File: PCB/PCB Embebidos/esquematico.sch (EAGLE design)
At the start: 14 parts, among them T1 BT138-V

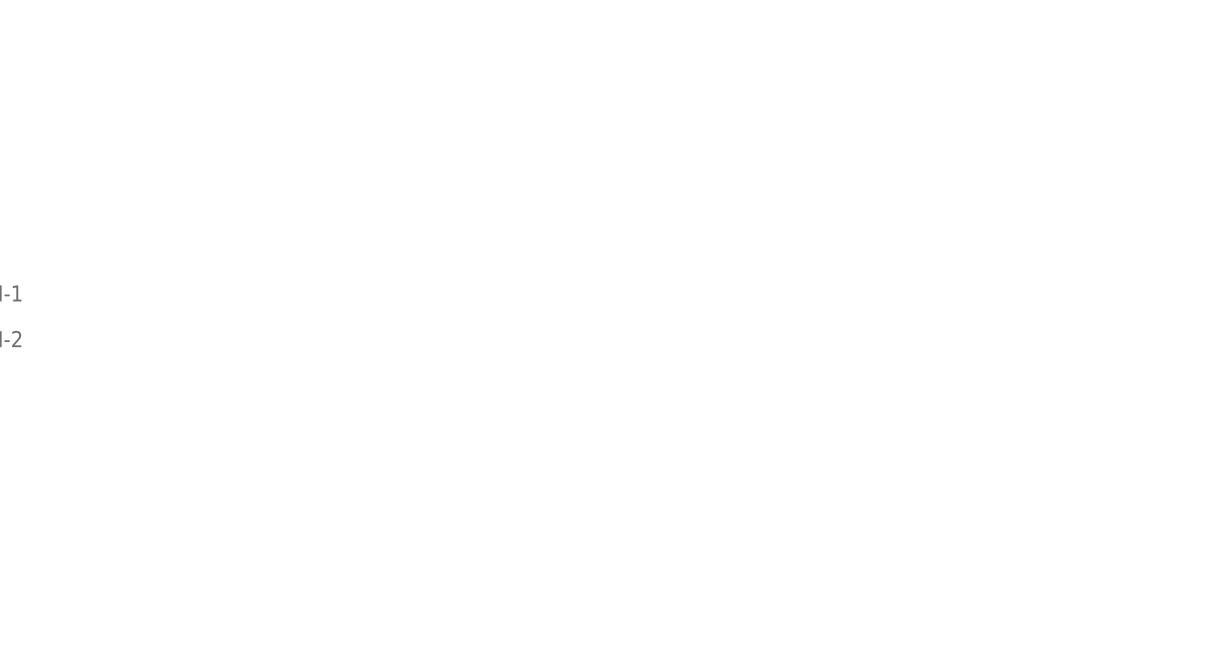
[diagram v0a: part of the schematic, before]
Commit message: Agregue el circuito de la termocupla al esquematico de Eagle. Falta definir si vamos a meter el PT100 como referencia
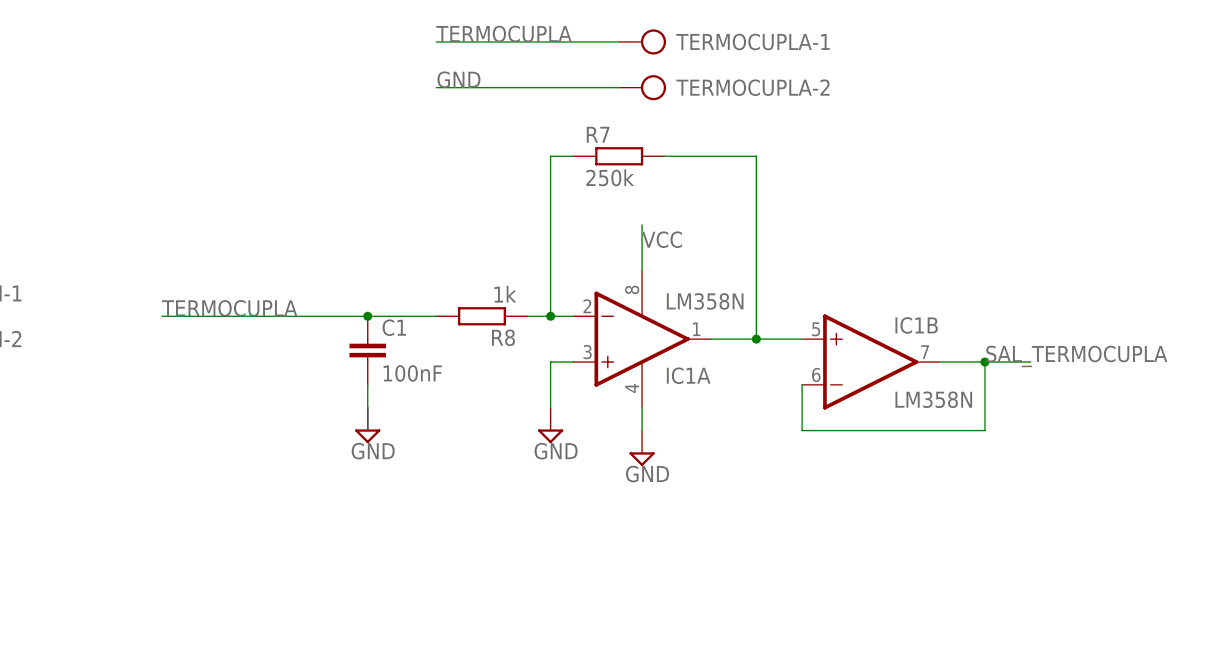
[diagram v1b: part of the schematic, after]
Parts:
- added C1: 100nF, capacitor-wima:C2,5-3
- added IC1: LM358N, linear:LM358N
- added R7: 250k, resistor:R-EU_0207/10
- added R8: 1k, resistor:R-EU_0207/10
- added TERMOCUPLA: (no value), con-ptr500:AK300/2
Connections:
- new net N$5: IC1A.-IN, R7.1, R8.1
- new net N$7: IC1A.OUT, IC1B.+IN, R7.2
- new net SAL_TERMOCUPLA: IC1B.-IN, IC1B.OUT
- new net TERMOCUPLA: C1.1, R8.2, TERMOCUPLA-1.KL
- net GND: now also C1.2, IC1A.+IN, IC1P.V-, TERMOCUPLA-2.KL
- net VCC: now also IC1P.V+
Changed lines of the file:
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@@
 <part name="ALIMENTACION" library="con-ptr500" deviceset="AK300/2" device=""/>
 <part name="PWM-FASE" library="con-ptr500" deviceset="AK300/2" device=""/>
+<part name="TERMOCUPLA" library="con-ptr500" deviceset="AK300/2" device=""/>
+<part name="IC1" library="linear" deviceset="LM358" device="N"/>
+<part name="R7" library="resistor" deviceset="R-EU_" device="0207/10" value="250k"/>
+<part name="C1" library="capacitor-wima" deviceset="C" device="2,5-3" value="100nF"/>
+<part name="R8" library="resistor" deviceset="R-EU_" device="0207/10" value="1k"/>
+<part name="SUPPLY2" library="supply2" deviceset="GND" device=""/>
+<part name="SUPPLY3" library="supply2" deviceset="GND" device=""/>
+<part name="SUPPLY4" library="supply2" deviceset="GND" device=""/>
 </parts>
 <sheets>
@@
 <instance part="PWM-FASE" gate="-1" x="109.22" y="111.76" rot="MR0"/>
 <instance part="PWM-FASE" gate="-2" x="109.22" y="106.68" rot="MR0"/>
+<instance part="TERMOCUPLA" gate="-1" x="200.66" y="124.46" rot="MR0"/>
+<instance part="TERMOCUPLA" gate="-2" x="200.66" y="119.38" rot="MR0"/>
+<instance part="IC1" gate="A" x="198.12" y="91.44" rot="MR180"/>
+<instance part="IC1" gate="B" x="223.52" y="88.9"/>
+<instance part="R7" gate="G$1" x="195.58" y="111.76"/>
+<instance part="C1" gate="G$1" x="167.64" y="91.44"/>
+<instance part="R8" gate="G$1" x="180.34" y="93.98" rot="R180"/>
+<instance part="SUPPLY2" gate="GND" x="167.64" y="81.28"/>
+<instance part="SUPPLY3" gate="GND" x="187.96" y="81.28"/>
+<instance part="IC1" gate="P" x="198.12" y="91.44"/>
+<instance part="SUPPLY4" gate="GND" x="198.12" y="78.74"/>
 </instances>
 <busses>
@@
 <wire x1="48.26" y1="48.26" x2="76.2" y2="48.26" width="0.1524" layer="91"/>
 <label x="48.26" y="48.26" size="1.778" layer="95"/>
+</segment>
+<segment>
+<pinref part="C1" gate="G$1" pin="2"/>
+<wire x1="167.64" y1="86.36" x2="167.64" y2="83.82" width="0.1524" layer="91"/>
+<wire x1="167.64" y1="81.28" x2="167.64" y2="83.82" width="0.1524" layer="91"/>
+<pinref part="SUPPLY2" gate="GND" pin="GND"/>
+</segment>
+<segment>
+<pinref part="TERMOCUPLA" gate="-2" pin="KL"/>
+<wire x1="195.58" y1="119.38" x2="175.26" y2="119.38" width="0.1524" layer="91"/>
+<label x="175.26" y="119.38" size="1.778" layer="95"/>
+</segment>
+<segment>
+<pinref part="IC1" gate="A" pin="+IN"/>
+<pinref part="SUPPLY3" gate="GND" pin="GND"/>
+<wire x1="190.5" y1="88.9" x2="187.96" y2="88.9" width="0.1524" layer="91"/>
+<wire x1="187.96" y1="88.9" x2="187.96" y2="83.82" width="0.1524" layer="91"/>
+</segment>
+<segment>
+<pinref part="IC1" gate="P" pin="V-"/>
+<pinref part="SUPPLY4" gate="GND" pin="GND"/>
+<wire x1="198.12" y1="81.28" x2="198.12" y2="83.82" width="0.1524" layer="91"/>
 </segment>
 </net>
@@
 <label x="71.12" y="124.46" size="1.778" layer="95"/>
 </segment>
+<segment>
+<pinref part="IC1" gate="P" pin="V+"/>
+<wire x1="198.12" y1="99.06" x2="198.12" y2="104.14" width="0.1524" layer="91"/>
+<label x="198.12" y="101.6" size="1.778" layer="95"/>
+</segment>
 </net>
 <net name="FASE" class="0">
@@
 </segment>
 </net>
+<net name="SAL_TERMOCUPLA" class="0">
+<segment>
+<pinref part="IC1" gate="B" pin="OUT"/>
+<wire x1="231.14" y1="88.9" x2="236.22" y2="88.9" width="0.1524" layer="91"/>
+<label x="236.22" y="88.9" size="1.778" layer="95"/>
+<pinref part="IC1" gate="B" pin="-IN"/>
+<wire x1="236.22" y1="88.9" x2="241.3" y2="88.9" width="0.1524" layer="91"/>
+<wire x1="215.9" y1="86.36" x2="215.9" y2="81.28" width="0.1524" layer="91"/>
+<wire x1="215.9" y1="81.28" x2="236.22" y2="81.28" width="0.1524" layer="91"/>
+<wire x1="236.22" y1="81.28" x2="236.22" y2="88.9" width="0.1524" layer="91"/>
+<junction x="236.22" y="88.9"/>
+</segment>
+</net>
+<net name="N$5" class="0">
+<segment>
+<pinref part="R8" gate="G$1" pin="1"/>
+<pinref part="IC1" gate="A" pin="-IN"/>
+<wire x1="185.42" y1="93.98" x2="187.96" y2="93.98" width="0.1524" layer="91"/>
+<pinref part="R7" gate="G$1" pin="1"/>
+<wire x1="187.96" y1="93.98" x2="190.5" y2="93.98" width="0.1524" layer="91"/>
+<wire x1="190.5" y1="111.76" x2="187.96" y2="111.76" width="0.1524" layer="91"/>
+<wire x1="187.96" y1="111.76" x2="187.96" y2="93.98" width="0.1524" layer="91"/>
+<junction x="187.96" y="93.98"/>
+</segment>
+</net>
+<net name="N$7" class="0">
+<segment>
+<pinref part="R7" gate="G$1" pin="2"/>
+<wire x1="200.66" y1="111.76" x2="210.82" y2="111.76" width="0.1524" layer="91"/>
+<wire x1="210.82" y1="111.76" x2="210.82" y2="91.44" width="0.1524" layer="91"/>
+<pinref part="IC1" gate="A" pin="OUT"/>
+<wire x1="210.82" y1="91.44" x2="205.74" y2="91.44" width="0.1524" layer="91"/>
+<pinref part="IC1" gate="B" pin="+IN"/>
+<wire x1="215.9" y1="91.44" x2="210.82" y2="91.44" width="0.1524" layer="91"/>
+<junction x="210.82" y="91.44"/>
+</segment>
+</net>
+<net name="TERMOCUPLA" class="0">
+<segment>
+<pinref part="TERMOCUPLA" gate="-1" pin="KL"/>
+<wire x1="195.58" y1="124.46" x2="175.26" y2="124.46" width="0.1524" layer="91"/>
+<label x="175.26" y="124.46" size="1.778" layer="95"/>
+</segment>
+<segment>
+<pinref part="R8" gate="G$1" pin="2"/>
+<pinref part="C1" gate="G$1" pin="1"/>
+<wire x1="175.26" y1="93.98" x2="167.64" y2="93.98" width="0.1524" layer="91"/>
+<wire x1="167.64" y1="93.98" x2="144.78" y2="93.98" width="0.1524" layer="91"/>
+<junction x="167.64" y="93.98"/>
+<label x="144.78" y="93.98" size="1.778" layer="95"/>
+</segment>
+</net>

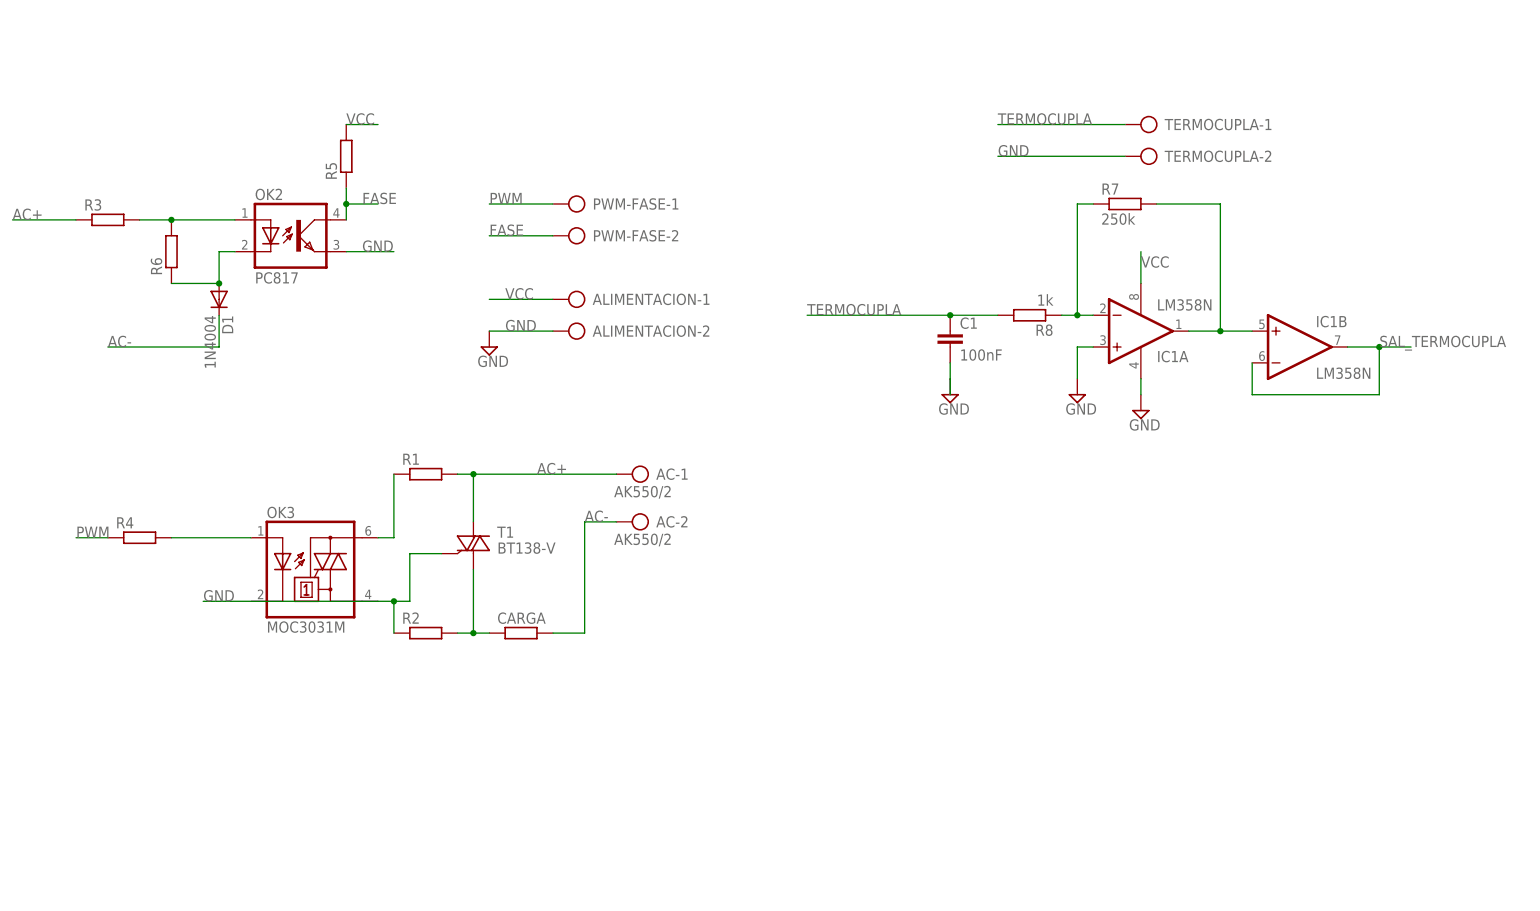
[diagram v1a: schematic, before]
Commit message: Agregue al PCB un regulador de 3.3v porque la EDU-CIAA labura con esa tension, y sino iba a tener problemas con el ADC. Tendria que probar que la parte de control siga funcionando bien, pero segun las hojas de datos no voy a tener ningun problema
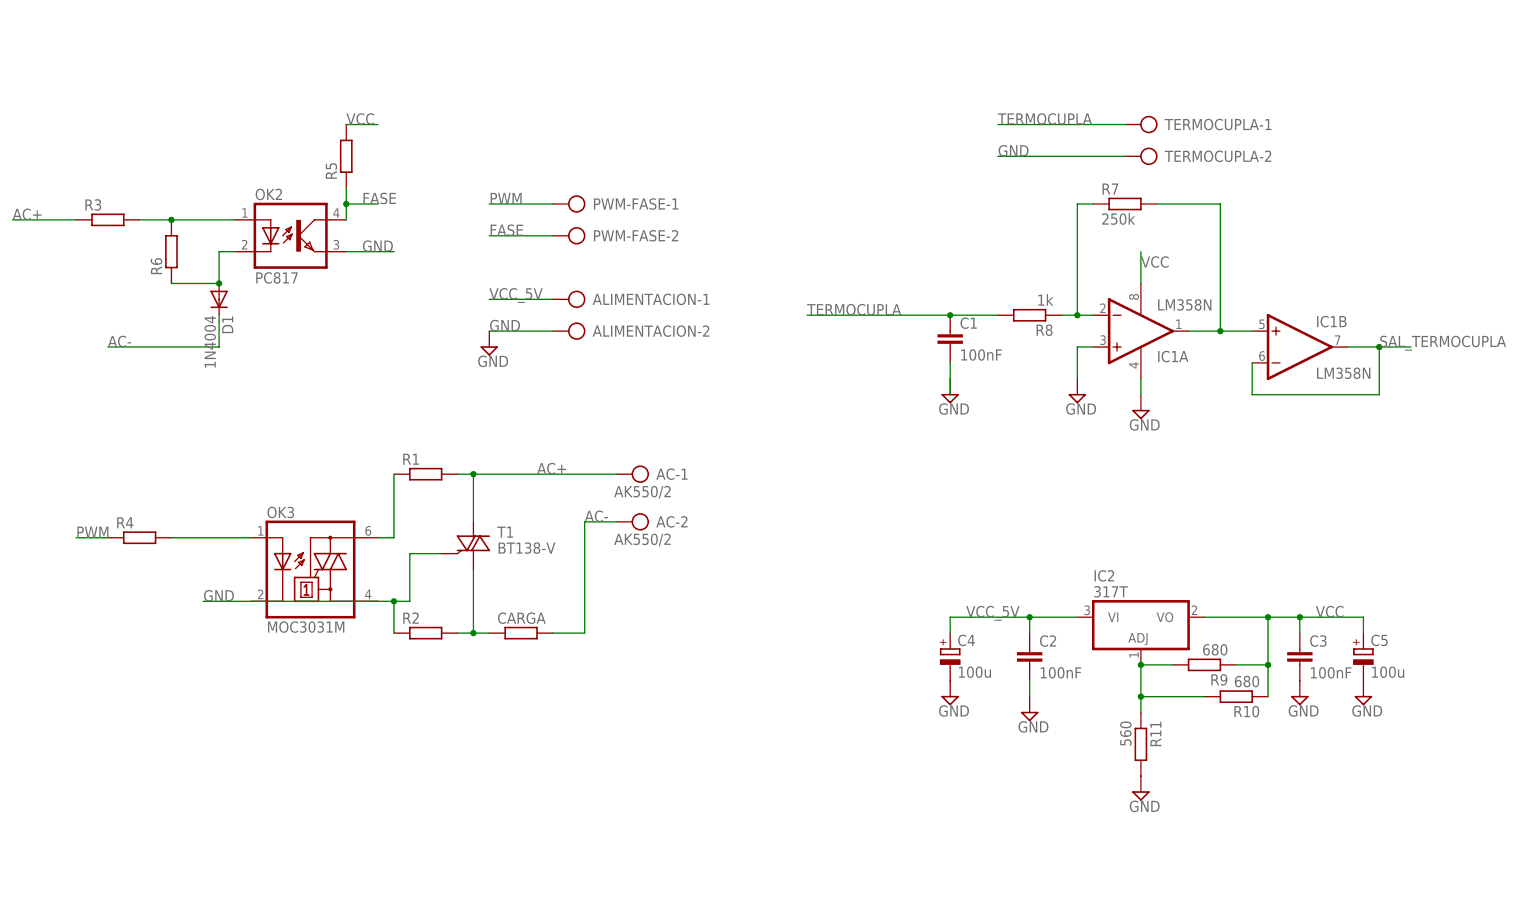
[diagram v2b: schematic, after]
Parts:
- added C2, C3: 100nF, capacitor-wima:C2,5-3
- added C4, C5: 100u, rcl:CPOL-EUE1.8-4
- added IC2: 317T, linear:317T
- added R10, R9: 680, resistor:R-EU_0207/10
- added R11: 560, resistor:R-EU_0207/10
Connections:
- new net N$6: IC2.ADJ, R10.2, R11.1, R9.2
- new net VCC_5V: ALIMENTACION-1.KL, C2.1, C4.+, IC2.VI
- net GND: now also C2.2, C3.2, C4.-, C5.-, R11.2
- net VCC: now also C3.1, C5.+, IC2.VO, R10.1, R9.1; no longer ALIMENTACION-1.KL
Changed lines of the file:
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@@
 <part name="SUPPLY3" library="supply2" deviceset="GND" device=""/>
 <part name="SUPPLY4" library="supply2" deviceset="GND" device=""/>
+<part name="IC2" library="linear" deviceset="*317" device="T"/>
+<part name="R9" library="resistor" deviceset="R-EU_" device="0207/10" value="680"/>
+<part name="R10" library="resistor" deviceset="R-EU_" device="0207/10" value="680"/>
+<part name="R11" library="resistor" deviceset="R-EU_" device="0207/10" value="560"/>
+<part name="C2" library="capacitor-wima" deviceset="C" device="2,5-3" value="100nF"/>
+<part name="C3" library="capacitor-wima" deviceset="C" device="2,5-3" value="100nF"/>
+<part name="SUPPLY5" library="supply2" deviceset="GND" device=""/>
+<part name="SUPPLY6" library="supply2" deviceset="GND" device=""/>
+<part name="SUPPLY7" library="supply2" deviceset="GND" device=""/>
+<part name="C4" library="rcl" deviceset="CPOL-EU" device="E1.8-4" value="100u"/>
+<part name="C5" library="rcl" deviceset="CPOL-EU" device="E1.8-4" value="100u"/>
+<part name="SUPPLY8" library="supply2" deviceset="GND" device=""/>
+<part name="SUPPLY9" library="supply2" deviceset="GND" device=""/>
 </parts>
 <sheets>
@@
 <instance part="IC1" gate="P" x="198.12" y="91.44"/>
 <instance part="SUPPLY4" gate="GND" x="198.12" y="78.74"/>
+<instance part="IC2" gate="A1" x="198.12" y="43.18"/>
+<instance part="R9" gate="G$1" x="208.28" y="38.1" rot="R180"/>
+<instance part="R10" gate="G$1" x="213.36" y="33.02" rot="R180"/>
+<instance part="R11" gate="G$1" x="198.12" y="25.4" rot="R270"/>
+<instance part="C2" gate="G$1" x="180.34" y="40.64"/>
+<instance part="C3" gate="G$1" x="223.52" y="40.64"/>
+<instance part="SUPPLY5" gate="GND" x="180.34" y="30.48"/>
+<instance part="SUPPLY6" gate="GND" x="223.52" y="33.02"/>
+<instance part="SUPPLY7" gate="GND" x="198.12" y="17.78"/>
+<instance part="C4" gate="G$1" x="167.64" y="40.64"/>
+<instance part="C5" gate="G$1" x="233.68" y="40.64"/>
+<instance part="SUPPLY8" gate="GND" x="167.64" y="33.02"/>
+<instance part="SUPPLY9" gate="GND" x="233.68" y="33.02"/>
 </instances>
 <busses>
@@
 <pinref part="ALIMENTACION" gate="-2" pin="KL"/>
 <wire x1="104.14" y1="91.44" x2="93.98" y2="91.44" width="0.1524" layer="91"/>
-<label x="96.52" y="91.44" size="1.778" layer="95"/>
+<label x="93.98" y="91.44" size="1.778" layer="95"/>
 <pinref part="SUPPLY1" gate="GND" pin="GND"/>
 </segment>
@@
 <pinref part="SUPPLY4" gate="GND" pin="GND"/>
 <wire x1="198.12" y1="81.28" x2="198.12" y2="83.82" width="0.1524" layer="91"/>
+</segment>
+<segment>
+<pinref part="C2" gate="G$1" pin="2"/>
+<pinref part="SUPPLY5" gate="GND" pin="GND"/>
+<wire x1="180.34" y1="33.02" x2="180.34" y2="35.56" width="0.1524" layer="91"/>
+</segment>
+<segment>
+<pinref part="C3" gate="G$1" pin="2"/>
+<pinref part="SUPPLY6" gate="GND" pin="GND"/>
+</segment>
+<segment>
+<pinref part="R11" gate="G$1" pin="2"/>
+<pinref part="SUPPLY7" gate="GND" pin="GND"/>
+</segment>
+<segment>
+<pinref part="C4" gate="G$1" pin="-"/>
+<pinref part="SUPPLY8" gate="GND" pin="GND"/>
+</segment>
+<segment>
+<pinref part="C5" gate="G$1" pin="-"/>
+<pinref part="SUPPLY9" gate="GND" pin="GND"/>
 </segment>
 </net>
@@
 <net name="VCC" class="0">
 <segment>
-<pinref part="ALIMENTACION" gate="-1" pin="KL"/>
-<wire x1="104.14" y1="96.52" x2="93.98" y2="96.52" width="0.1524" layer="91"/>
-<label x="96.52" y="96.52" size="1.778" layer="95"/>
-</segment>
-<segment>
 <pinref part="R5" gate="G$1" pin="2"/>
 <wire x1="71.12" y1="124.46" x2="76.2" y2="124.46" width="0.1524" layer="91"/>
@@
 <wire x1="198.12" y1="99.06" x2="198.12" y2="104.14" width="0.1524" layer="91"/>
 <label x="198.12" y="101.6" size="1.778" layer="95"/>
+</segment>
+<segment>
+<pinref part="IC2" gate="A1" pin="VO"/>
+<wire x1="208.28" y1="45.72" x2="218.44" y2="45.72" width="0.1524" layer="91"/>
+<pinref part="C3" gate="G$1" pin="1"/>
+<wire x1="218.44" y1="45.72" x2="223.52" y2="45.72" width="0.1524" layer="91"/>
+<wire x1="223.52" y1="45.72" x2="223.52" y2="43.18" width="0.1524" layer="91"/>
+<pinref part="R9" gate="G$1" pin="1"/>
+<wire x1="213.36" y1="38.1" x2="218.44" y2="38.1" width="0.1524" layer="91"/>
+<wire x1="218.44" y1="38.1" x2="218.44" y2="45.72" width="0.1524" layer="91"/>
+<junction x="218.44" y="45.72"/>
+<pinref part="R10" gate="G$1" pin="1"/>
+<wire x1="218.44" y1="33.02" x2="218.44" y2="38.1" width="0.1524" layer="91"/>
+<junction x="218.44" y="38.1"/>
+<wire x1="223.52" y1="45.72" x2="233.68" y2="45.72" width="0.1524" layer="91"/>
+<junction x="223.52" y="45.72"/>
+<pinref part="C5" gate="G$1" pin="+"/>
+<wire x1="233.68" y1="45.72" x2="233.68" y2="43.18" width="0.1524" layer="91"/>
+<label x="226.06" y="45.72" size="1.778" layer="95"/>
 </segment>
 </net>
@@
 </segment>
 </net>
+<net name="N$6" class="0">
+<segment>
+<pinref part="R11" gate="G$1" pin="1"/>
+<pinref part="IC2" gate="A1" pin="ADJ"/>
+<wire x1="198.12" y1="30.48" x2="198.12" y2="33.02" width="0.1524" layer="91"/>
+<pinref part="R9" gate="G$1" pin="2"/>
+<wire x1="198.12" y1="33.02" x2="198.12" y2="38.1" width="0.1524" layer="91"/>
+<wire x1="203.2" y1="38.1" x2="198.12" y2="38.1" width="0.1524" layer="91"/>
+<junction x="198.12" y="38.1"/>
+<pinref part="R10" gate="G$1" pin="2"/>
+<wire x1="208.28" y1="33.02" x2="198.12" y2="33.02" width="0.1524" layer="91"/>
+<junction x="198.12" y="33.02"/>
+</segment>
+</net>
+<net name="VCC_5V" class="0">
+<segment>
+<pinref part="ALIMENTACION" gate="-1" pin="KL"/>
+<wire x1="104.14" y1="96.52" x2="93.98" y2="96.52" width="0.1524" layer="91"/>
+<label x="93.98" y="96.52" size="1.778" layer="95"/>
+</segment>
+<segment>
+<pinref part="IC2" gate="A1" pin="VI"/>
+<wire x1="187.96" y1="45.72" x2="180.34" y2="45.72" width="0.1524" layer="91"/>
+<pinref part="C2" gate="G$1" pin="1"/>
+<wire x1="180.34" y1="45.72" x2="180.34" y2="43.18" width="0.1524" layer="91"/>
+<pinref part="C4" gate="G$1" pin="+"/>
+<wire x1="167.64" y1="43.18" x2="167.64" y2="45.72" width="0.1524" layer="91"/>
+<wire x1="167.64" y1="45.72" x2="180.34" y2="45.72" width="0.1524" layer="91"/>
+<junction x="180.34" y="45.72"/>
+<label x="170.18" y="45.72" size="1.778" layer="95"/>
+</segment>
+</net>
